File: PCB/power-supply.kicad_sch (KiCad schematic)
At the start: 16 parts, among them J2 DF63-5P-3.96DSA

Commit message: re-annotate schematic
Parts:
- renumbered DBG31 to DBG1, DBG32 to DBG2, DBG33 to DBG3, DBG34 to DBG4, DBG35 to DBG5, DBG1 to DBG6
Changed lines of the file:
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@@
   (symbol (lib_id "Oro:DebugPin") (at 59.055 100.33 180) (unit 1)
     (in_bom no) (on_board yes) (dnp no)
-    (property "Reference" "DBG32" (at 53.34 100.33 0)
+    (property "Reference" "DBG2" (at 53.34 100.33 0)
       (effects (font (size 1.27 1.27)) hide)
     )
@@
       (project "OroLink"
         (path "/e89dcd22-1250-4a5b-b778-1c95a0dd623d/f955395e-bf1a-4ef3-9cfe-ec9d49f66988"
-          (reference "DBG32") (unit 1)
+          (reference "DBG2") (unit 1)
         )
       )
@@
       (project "OroLink"
         (path "/e89dcd22-1250-4a5b-b778-1c95a0dd623d/f955395e-bf1a-4ef3-9cfe-ec9d49f66988"
-          (reference "#PWR025") (unit 1)
+          (reference "#PWR024") (unit 1)
         )
       )
@@
       (project "OroLink"
         (path "/e89dcd22-1250-4a5b-b778-1c95a0dd623d/f955395e-bf1a-4ef3-9cfe-ec9d49f66988"
-          (reference "C19") (unit 1)
+          (reference "C22") (unit 1)
         )
       )
@@
   (symbol (lib_id "Oro:DebugPin") (at 59.055 102.87 180) (unit 1)
     (in_bom no) (on_board yes) (dnp no)
-    (property "Reference" "DBG33" (at 53.34 102.87 0)
+    (property "Reference" "DBG3" (at 53.34 102.87 0)
       (effects (font (size 1.27 1.27)) hide)
     )
@@
       (project "OroLink"
         (path "/e89dcd22-1250-4a5b-b778-1c95a0dd623d/f955395e-bf1a-4ef3-9cfe-ec9d49f66988"
-          (reference "DBG33") (unit 1)
+          (reference "DBG3") (unit 1)
         )
       )
@@
   (symbol (lib_id "Oro:DebugPin") (at 264.16 98.425 0) (unit 1)
     (in_bom no) (on_board yes) (dnp no)
-    (property "Reference" "DBG1" (at 269.875 98.425 0)
+    (property "Reference" "DBG6" (at 269.875 98.425 0)
       (effects (font (size 1.27 1.27)) hide)
     )
@@
       (project "OroLink"
         (path "/e89dcd22-1250-4a5b-b778-1c95a0dd623d/f955395e-bf1a-4ef3-9cfe-ec9d49f66988"
-          (reference "DBG1") (unit 1)
+          (reference "DBG6") (unit 1)
         )
       )
@@
       (project "OroLink"
         (path "/e89dcd22-1250-4a5b-b778-1c95a0dd623d/f955395e-bf1a-4ef3-9cfe-ec9d49f66988"
-          (reference "#PWR021") (unit 1)
+          (reference "#PWR020") (unit 1)
         )
       )
@@
       (project "OroLink"
         (path "/e89dcd22-1250-4a5b-b778-1c95a0dd623d/f955395e-bf1a-4ef3-9cfe-ec9d49f66988"
-          (reference "#PWR024") (unit 1)
+          (reference "#PWR023") (unit 1)
         )
       )
@@
       (project "OroLink"
         (path "/e89dcd22-1250-4a5b-b778-1c95a0dd623d/f955395e-bf1a-4ef3-9cfe-ec9d49f66988"
-          (reference "#PWR023") (unit 1)
+          (reference "#PWR022") (unit 1)
         )
       )
@@
   (symbol (lib_id "Oro:DebugPin") (at 59.055 105.41 180) (unit 1)
     (in_bom no) (on_board yes) (dnp no)
-    (property "Reference" "DBG34" (at 53.34 105.41 0)
+    (property "Reference" "DBG4" (at 53.34 105.41 0)
       (effects (font (size 1.27 1.27)) hide)
     )
@@
       (project "OroLink"
         (path "/e89dcd22-1250-4a5b-b778-1c95a0dd623d/f955395e-bf1a-4ef3-9cfe-ec9d49f66988"
-          (reference "DBG34") (unit 1)
+          (reference "DBG4") (unit 1)
         )
       )
@@
   (symbol (lib_id "Oro:DebugPin") (at 195.58 100.965 180) (unit 1)
     (in_bom no) (on_board yes) (dnp no)
-    (property "Reference" "DBG35" (at 189.865 100.965 0)
+    (property "Reference" "DBG5" (at 189.865 100.965 0)
       (effects (font (size 1.27 1.27)) hide)
     )
@@
       (project "OroLink"
         (path "/e89dcd22-1250-4a5b-b778-1c95a0dd623d/f955395e-bf1a-4ef3-9cfe-ec9d49f66988"
-          (reference "DBG35") (unit 1)
+          (reference "DBG5") (unit 1)
         )
       )
@@
   (symbol (lib_id "Oro:DebugPin") (at 59.055 97.79 180) (unit 1)
     (in_bom no) (on_board yes) (dnp no)
-    (property "Reference" "DBG31" (at 53.34 97.79 0)
+    (property "Reference" "DBG1" (at 53.34 97.79 0)
       (effects (font (size 1.27 1.27)) hide)
     )
@@
       (project "OroLink"
         (path "/e89dcd22-1250-4a5b-b778-1c95a0dd623d/f955395e-bf1a-4ef3-9cfe-ec9d49f66988"
-          (reference "DBG31") (unit 1)
+          (reference "DBG1") (unit 1)
         )
       )
@@
       (project "OroLink"
         (path "/e89dcd22-1250-4a5b-b778-1c95a0dd623d/f955395e-bf1a-4ef3-9cfe-ec9d49f66988"
-          (reference "C20") (unit 1)
+          (reference "C23") (unit 1)
         )
       )
@@
       (project "OroLink"
         (path "/e89dcd22-1250-4a5b-b778-1c95a0dd623d/f955395e-bf1a-4ef3-9cfe-ec9d49f66988"
-          (reference "C18") (unit 1)
+          (reference "C21") (unit 1)
         )
       )
@@
       (project "OroLink"
         (path "/e89dcd22-1250-4a5b-b778-1c95a0dd623d/f955395e-bf1a-4ef3-9cfe-ec9d49f66988"
-          (reference "#PWR020") (unit 1)
+          (reference "#PWR019") (unit 1)
         )
       )
@@
       (project "OroLink"
         (path "/e89dcd22-1250-4a5b-b778-1c95a0dd623d/f955395e-bf1a-4ef3-9cfe-ec9d49f66988"
-          (reference "#PWR019") (unit 1)
+          (reference "#PWR018") (unit 1)
         )
       )
@@
       (project "OroLink"
         (path "/e89dcd22-1250-4a5b-b778-1c95a0dd623d/f955395e-bf1a-4ef3-9cfe-ec9d49f66988"
-          (reference "#PWR022") (unit 1)
-        )
-      )
+          (reference "#PWR021") (unit 1)
+        )
+      )

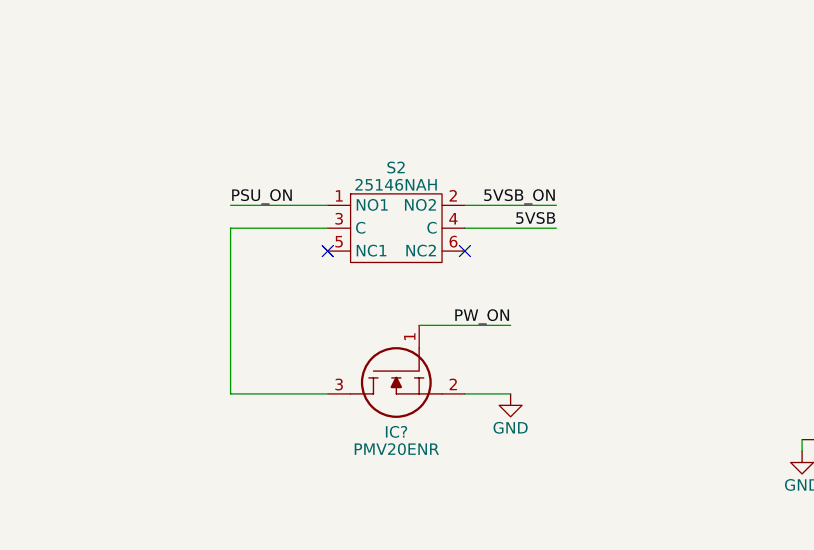
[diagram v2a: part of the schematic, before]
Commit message: add pullup/down resistors and fix oro 6p lines with boot1/0
closes #24
closes #21
closes #15
closes #12
closes #6
closes #3
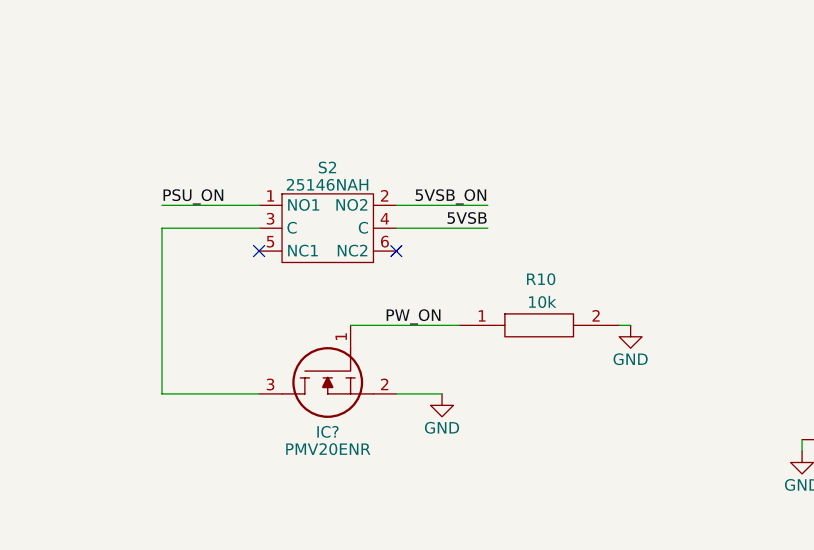
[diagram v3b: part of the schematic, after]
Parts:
- added R10: 10k, SamacSys_Parts:RESC5025X65N, symbol SamacSys_Parts:RC2010JK-0710KL
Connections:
- net GND: now also R10.2
- net SYS_PWR_ON: now also R10.1
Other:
- moved on the sheet: IC?, S2

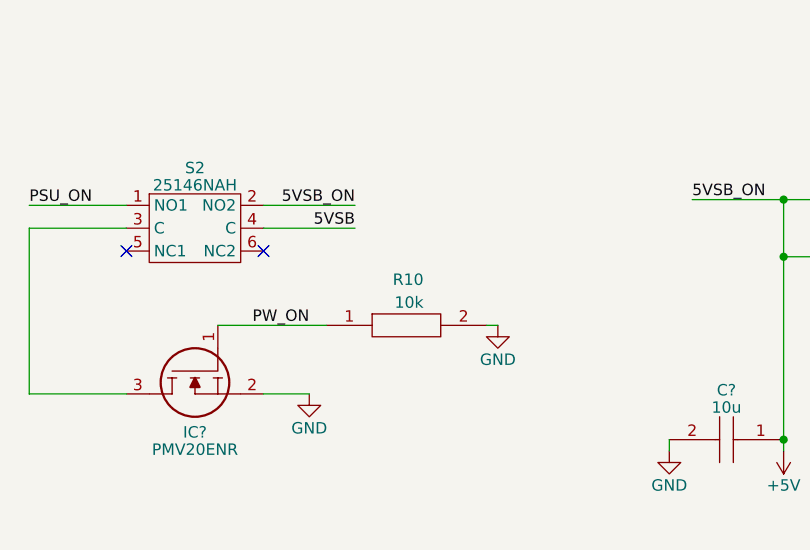
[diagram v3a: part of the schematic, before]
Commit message: switch 10k and 4.7k resistors to smaller packages (closes #32)
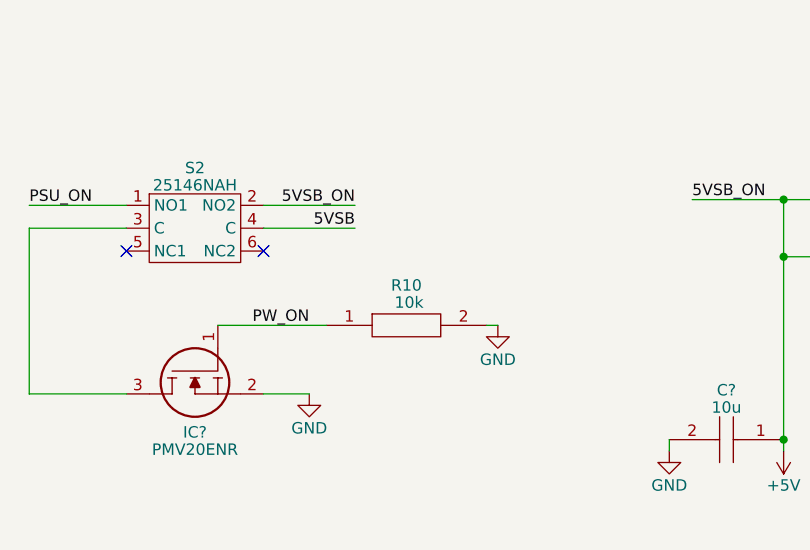
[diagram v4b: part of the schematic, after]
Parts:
- R10: footprint SamacSys_Parts:RESC5025X65N -> RESC5025X65N
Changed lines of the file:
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@@
   (symbol (lib_id "SamacSys_Parts:RC2010JK-0710KL") (at 137.16 106.045 0) (unit 1)
     (in_bom yes) (on_board yes) (dnp no)
-    (property "Reference" "R10" (at 147.955 100.965 0)
-      (effects (font (size 1.27 1.27)) (justify right))
+    (property "Reference" "R10" (at 146.05 101.6 0)
+      (effects (font (size 1.27 1.27)))
     )
     (property "Value" "10k" (at 147.955 103.505 0)
       (effects (font (size 1.27 1.27)) (justify right))
     )
-    (property "Footprint" "SamacSys_Parts:RESC5025X65N" (at 151.13 104.775 0)
+    (property "Footprint" "RESC5025X65N" (at 151.13 104.775 0)
       (effects (font (size 1.27 1.27)) (justify left) hide)
     )
@@
       (effects (font (size 1.27 1.27)))
     )
-    (property "Footprint" "SamacSys_Parts:RESC5025X65N" (at 212.09 90.805 0)
-      (effects (font (size 1.27 1.27)) (justify left) hide)
-    )
+    (property "Footprint" "RESC5025X65N" (at 212.09 90.805 0)
+      (effects (font (size 1.27 1.27)) (justify left) hide)
+    )

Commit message: actually reduce 10k package size (ref #32)
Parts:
- R10: footprint RESC5025X65N -> RESC1005X40N; symbol SamacSys_Parts:RC2010JK-0710KL -> SamacSys_Parts:RK73H1ETTP1002F; Arrow Part Number RC2010JK-0710KL -> RK73H1ETTP1002F; Arrow Price/Stock https://www.arrow.com/en/products/rc2010jk-0710kl/yageo -> https://www.arrow.com/en/products/rk73h1ettp1002f/koa-speer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; Height 0.65 -> 0.4; Manufacturer_Name KEMET -> KOA Speer; Manufacturer_Part_Number RC2010JK-0710KL -> RK73H1ETTP1002F; Mouser Part Number 603-RC2010JK-0710KL -> 660-RK73H1ETTP1002F; Mouser Price/Stock https://www.mouser.co.uk/ProductDetail/YAGEO/RC2010JK-0710K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 -> https://www.mouser.co.uk/ProductDetail/KOA-Speer/RK73H1ETTP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
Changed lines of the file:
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@@
     )
   )
-  (symbol (lib_id "SamacSys_Parts:RC2010JK-0710KL") (at 137.16 106.045 0) (unit 1)
+  (symbol (lib_id "SamacSys_Parts:RK73H1ETTP1002F") (at 137.16 106.045 0) (unit 1)
     (in_bom yes) (on_board yes) (dnp no)
     (property "Reference" "R10" (at 146.05 101.6 0)
@@
       (effects (font (size 1.27 1.27)) (justify right))
     )
-    (property "Footprint" "RESC5025X65N" (at 151.13 104.775 0)
-      (effects (font (size 1.27 1.27)) (justify left) hide)
-    )
-    (property "Datasheet" "https://www.arrow.com/en/products/rc2010jk-0710kl/yageo" (at 151.13 107.315 0)
-      (effects (font (size 1.27 1.27)) (justify left) hide)
-    )
-    (property "Description" "Res Thick Film 2010 10K Ohm 5% 0.75W(3/4W) +/-100ppm/C Pad SMD T/R" (at 151.13 109.855 0)
-      (effects (font (size 1.27 1.27)) (justify left) hide)
-    )
-    (property "Height" "0.65" (at 151.13 112.395 0)
-      (effects (font (size 1.27 1.27)) (justify left) hide)
-    )
-    (property "Manufacturer_Name" "KEMET" (at 151.13 114.935 0)
-      (effects (font (size 1.27 1.27)) (justify left) hide)
-    )
-    (property "Manufacturer_Part_Number" "RC2010JK-0710KL" (at 151.13 117.475 0)
-      (effects (font (size 1.27 1.27)) (justify left) hide)
-    )
-    (property "Mouser Part Number" "603-RC2010JK-0710KL" (at 151.13 120.015 0)
-      (effects (font (size 1.27 1.27)) (justify left) hide)
-    )
-    (property "Mouser Price/Stock" "https://www.mouser.co.uk/ProductDetail/YAGEO/RC2010JK-0710KL?qs=sNpmnPgvziOLj5uuquGIow%3D%3D" (at 151.13 122.555 0)
-      (effects (font (size 1.27 1.27)) (justify left) hide)
-    )
-    (property "Arrow Part Number" "RC2010JK-0710KL" (at 151.13 125.095 0)
-      (effects (font (size 1.27 1.27)) (justify left) hide)
-    )
-    (property "Arrow Price/Stock" "https://www.arrow.com/en/products/rc2010jk-0710kl/yageo" (at 151.13 127.635 0)
+    (property "Footprint" "RESC1005X40N" (at 151.13 104.775 0)
+      (effects (font (size 1.27 1.27)) (justify left) hide)
+    )
+    (property "Datasheet" "http://www.koaspeer.com/catimages/Products/RK73-RT/RK73-RT.pdf" (at 151.13 107.315 0)
+      (effects (font (size 1.27 1.27)) (justify left) hide)
+    )
+    (property "Description" "Resistor,ThickFilm1005,0.063W,10kohm" (at 151.13 109.855 0)
+      (effects (font (size 1.27 1.27)) (justify left) hide)
+    )
+    (property "Height" "0.4" (at 151.13 112.395 0)
+      (effects (font (size 1.27 1.27)) (justify left) hide)
+    )
+    (property "Manufacturer_Name" "KOA Speer" (at 151.13 114.935 0)
+      (effects (font (size 1.27 1.27)) (justify left) hide)
+    )
+    (property "Manufacturer_Part_Number" "RK73H1ETTP1002F" (at 151.13 117.475 0)
+      (effects (font (size 1.27 1.27)) (justify left) hide)
+    )
+    (property "Mouser Part Number" "660-RK73H1ETTP1002F" (at 151.13 120.015 0)
+      (effects (font (size 1.27 1.27)) (justify left) hide)
+    )
+    (property "Mouser Price/Stock" "https://www.mouser.co.uk/ProductDetail/KOA-Speer/RK73H1ETTP1002F?qs=uLfVlVfCHH2OZ4JTybrBPQ%3D%3D" (at 151.13 122.555 0)
+      (effects (font (size 1.27 1.27)) (justify left) hide)
+    )
+    (property "Arrow Part Number" "RK73H1ETTP1002F" (at 151.13 125.095 0)
+      (effects (font (size 1.27 1.27)) (justify left) hide)
+    )
+    (property "Arrow Price/Stock" "https://www.arrow.com/en/products/rk73h1ettp1002f/koa-speer-electronics?region=nac" (at 151.13 127.635 0)
       (effects (font (size 1.27 1.27)) (justify left) hide)
     )
@@
     )
   )
-  (symbol (lib_id "SamacSys_Parts:RC2010JK-0710KL") (at 198.12 92.075 0) (unit 1)
+  (symbol (lib_id "SamacSys_Parts:RK73H1ETTP1002F") (at 198.12 92.075 0) (unit 1)
     (in_bom yes) (on_board yes) (dnp no)
     (property "Reference" "R10" (at 207.01 88.265 0)
@@
       (effects (font (size 1.27 1.27)))
     )
-    (property "Footprint" "RESC5025X65N" (at 212.09 90.805 0)
-      (effects (font (size 1.27 1.27)) (justify left) hide)
-    )
-    (property "Datasheet" "https://www.arrow.com/en/products/rc2010jk-0710kl/yageo" (at 212.09 93.345 0)
-      (effects (font (size 1.27 1.27)) (justify left) hide)
-    )
-    (property "Description" "Res Thick Film 2010 10K Ohm 5% 0.75W(3/4W) +/-100ppm/C Pad SMD T/R" (at 212.09 95.885 0)
-      (effects (font (size 1.27 1.27)) (justify left) hide)
-    )
-    (property "Height" "0.65" (at 212.09 98.425 0)
-      (effects (font (size 1.27 1.27)) (justify left) hide)
-    )
-    (property "Manufacturer_Name" "KEMET" (at 212.09 100.965 0)
-      (effects (font (size 1.27 1.27)) (justify left) hide)
-    )
-    (property "Manufacturer_Part_Number" "RC2010JK-0710KL" (at 212.09 103.505 0)
-      (effects (font (size 1.27 1.27)) (justify left) hide)
-    )
-    (property "Mouser Part Number" "603-RC2010JK-0710KL" (at 212.09 106.045 0)
-      (effects (font (size 1.27 1.27)) (justify left) hide)
-    )
-    (property "Mouser Price/Stock" "https://www.mouser.co.uk/ProductDetail/YAGEO/RC2010JK-0710KL?qs=sNpmnPgvziOLj5uuquGIow%3D%3D" (at 212.09 108.585 0)
-      (effects (font (size 1.27 1.27)) (justify left) hide)
-    )
-    (property "Arrow Part Number" "RC2010JK-0710KL" (at 212.09 111.125 0)
-      (effects (font (size 1.27 1.27)) (justify left) hide)
-    )
-    (property "Arrow Price/Stock" "https://www.arrow.com/en/products/rc2010jk-0710kl/yageo" (at 212.09 113.665 0)
-      (effects (font (size 1.27 1.27)) (justify left) hide)
-    )
+    (property "Footprint" "RESC1005X40N" (at 212.09 90.805 0)
+      (effects (font (size 1.27 1.27)) (justify left) hide)
+    )
+    (property "Datasheet" "http://www.koaspeer.com/catimages/Products/RK73-RT/RK73-RT.pdf" (at 212.09 93.345 0)
+      (effects (font (size 1.27 1.27)) (justify left) hide)
+    )
+    (property "Description" "Resistor,ThickFilm1005,0.063W,10kohm" (at 212.09 95.885 0)
+      (effects (font (size 1.27 1.27)) (justify left) hide)
+    )
+    (property "Height" "0.4" (at 212.09 98.425 0)
+      (effects (font (size 1.27 1.27)) (justify left) hide)
+    )
+    (property "Manufacturer_Name" "KOA Speer" (at 212.09 100.965 0)
+      (effects (font (size 1.27 1.27)) (justify left) hide)
+    )
+    (property "Manufacturer_Part_Number" "RK73H1ETTP1002F" (at 212.09 103.505 0)
+      (effects (font (size 1.27 1.27)) (justify left) hide)
+    )
+    (property "Mouser Part Number" "660-RK73H1ETTP1002F" (at 212.09 106.045 0)
+      (effects (font (size 1.27 1.27)) (justify left) hide)
+    )
+    (property "Mouser Price/Stock" "https://www.mouser.co.uk/ProductDetail/KOA-Speer/RK73H1ETTP1002F?qs=uLfVlVfCHH2OZ4JTybrBPQ%3D%3D" (at 212.09 108.585 0)
+      (effects (font (size 1.27 1.27)) (justify left) hide)
+    )
+    (property "Arrow Part Number" "RK73H1ETTP1002F" (at 212.09 111.125 0)
+      (effects (font (size 1.27 1.27)) (justify left) hide)
+    )
+    (property "Arrow Price/Stock" "https://www.arrow.com/en/products/rk73h1ettp1002f/koa-speer-electronics?region=nac" (at 212.09 113.665 0)
+      (effects (font (size 1.27 1.27)) (justify left) hide)
+    )

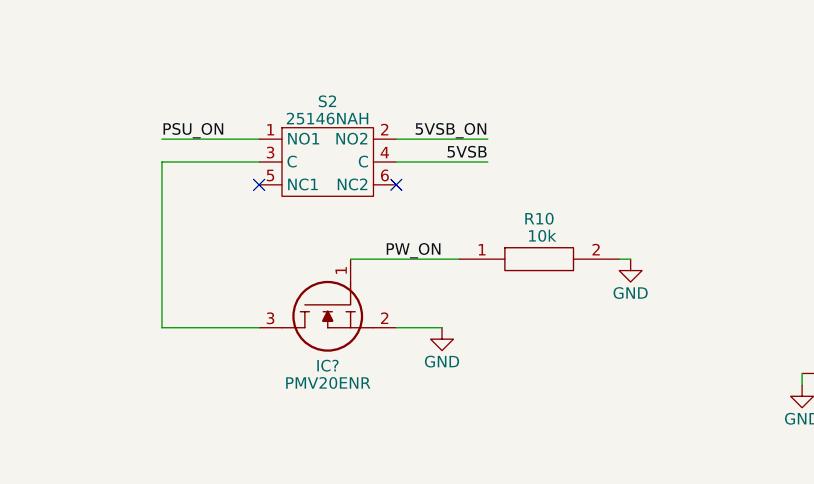
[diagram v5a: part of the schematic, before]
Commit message: redo pinout of entire MCU (closes #34)
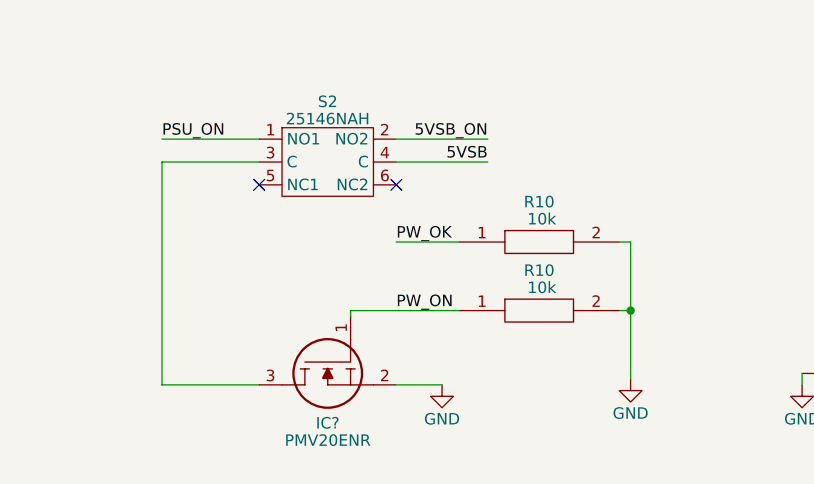
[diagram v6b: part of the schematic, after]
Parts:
- added R10: 10k, RESC1005X40N, symbol SamacSys_Parts:RK73H1ETTP1002F
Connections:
- net GND: now also R10.2
- net PWR_OK: now also R10.1
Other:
- moved on the sheet: IC?, R10

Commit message: most power routing completed
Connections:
- net +5V: now also S2.4 (C); no longer S2.2 (NO2)
- net 5VSB: now also S2.2 (NO2); no longer S2.4 (C)
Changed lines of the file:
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@@
     (stroke (width 0) (type default))
   )
-  (wire (pts (xy 130.175 92.71) (xy 140.335 92.71))
+  (wire (pts (xy 130.175 95.25) (xy 140.335 95.25))
     (stroke (width 0) (type default))
   )
@@
     (stroke (width 0) (type default))
   )
-  (wire (pts (xy 130.175 95.25) (xy 140.335 95.25))
+  (wire (pts (xy 130.175 92.71) (xy 140.335 92.71))
     (stroke (width 0) (type default))
   )
@@
     (effects (font (size 1.27 1.27)) (justify left bottom))
   )
-  (label "5VSB" (at 140.335 95.25 180) (fields_autoplaced)
+  (label "5VSB" (at 140.335 92.71 180) (fields_autoplaced)
     (effects (font (size 1.27 1.27)) (justify right bottom))
   )
@@
     (effects (font (size 1.27 1.27)) (justify left bottom))
   )
-  (label "5VSB_ON" (at 140.335 92.71 180) (fields_autoplaced)
+  (label "5VSB_ON" (at 140.335 95.25 180) (fields_autoplaced)
     (effects (font (size 1.27 1.27)) (justify right bottom))
   )
@@
     )
   )
-  (netclass_flag "" (length 2.54) (shape round) (at 140.335 95.25 270)
+  (netclass_flag "" (length 2.54) (shape round) (at 140.335 92.71 270)
     (effects (font (size 1.27 1.27)) (justify right bottom))
-    (property "Netclass" "5V" (at 144.145 95.25 0)
+    (property "Netclass" "5V" (at 144.145 92.71 0)
       (effects (font (size 1.27 1.27) italic) (justify left))
     )
